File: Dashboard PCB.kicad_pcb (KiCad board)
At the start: 2 copper layers, 200 x 100 mm, 62 parts, among them J1 Controls_Leader_Export_02x06, J2 CAN, J3 INDICATOR_SWITCH_OUT, J4 FAN_CTRL_01x02, J5 Horn_In_01x02, J6 Horn_Out_01x02, J7 CAN

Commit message: Routed
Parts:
- moved +12V 12.7 mm to (105.2, 51.5)
- moved C10 12.7 mm to (107.2, 54.5)
- moved C11 12.7 mm to (103.2, 54.5)
- moved GND 12.7 mm to (105.2, 57.5)
- moved DBG_LED 6.68 mm to (91.0, 59.1)
- moved Heartbeat_LED 6.68 mm to (91.0, 55.1)
- moved R12 6.68 mm to (90.0, 51.1)
- moved D3 0.79 mm to (79.5, 113.0)
- moved FAN_CTRL 0.32 mm to (83.0, 110.0)
- moved FWD_SW 0.30 mm to (163.0, 102.5)
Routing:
- net /LFT_OUT: track 320.8 -> 223.5 mm
- net /RT_OUT: track 296.0 -> 204.3 mm
- net /FWD_SW: track 177.7 -> 118.2 mm, vias 0 -> 2
- net /CRUZ_SET: track 274.2 -> 224.0 mm, vias 0 -> 2
- net /CRUZ_EN: track 184.1 -> 228.0 mm, vias 0 -> 2
- net /BPS_HZD: track 278.8 -> 254.5 mm
- net /IGN_PWR: track 195.6 -> 219.0 mm
- net /CANGND: track 17.8 -> 0.00 mm
- net /CAN+12V: track 17.8 -> 0.00 mm
- net /FAN+: track 26.7 -> 9.70 mm
- net /CAN-H: track 16.5 -> 0.00 mm
- net /FAN-: track 22.2 -> 5.77 mm
- net /CAN-L: track 16.2 -> 0.00 mm
- net /IGN_ARR: track 232.0 -> 220.5 mm
- net /DBG_LED: track 13.8 -> 22.2 mm
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- added copper zone on F.Cu, net /CAN+12V
- added copper zone on F.Cu, net /CAN-H
- added copper zone on B.Cu, net /CAN-L
- added copper zone on B.Cu, net /CANGND
- added copper zone on F.Cu, net /FAN+
- added copper zone on B.Cu, net /FAN-

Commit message: changed routing
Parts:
- moved C3 14.9 mm to (164.2, 101.5), turned to -90 degrees
- moved C4 14.4 mm to (164.2, 109.8), turned to -90 degrees
- moved REV_SW 12.0 mm to (151.0, 108.8)
- moved FWD_SW 12.0 mm to (151.0, 102.5)
- moved R4 11.4 mm to (161.2, 109.8), turned to -90 degrees
- moved R3 11.3 mm to (161.2, 101.5), turned to -90 degrees
- moved IGN_ARR 4.61 mm to (231.5, 92.0)
- moved C5 2.75 mm to (228.2, 93.0)
- moved R5 2.00 mm to (224.0, 93.0)
- moved C6 1.60 mm to (218.0, 91.8)
- moved IGN_PWR 1.03 mm to (212.0, 86.8)
- moved R6 1.03 mm to (214.8, 89.0)
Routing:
- net /IGN_ARR: track 220.5 -> 217.4 mm
- net /IGN_PWR: track 219.0 -> 216.5 mm
- net /FWD_SW: track 118.2 -> 119.8 mm
- net /REV_SW: track 127.1 -> 126.4 mm

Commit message: More stuff
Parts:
- J2: value CAN -> Conn_02x03_CAN
- J7: value CAN -> Conn_02x03_CAN; footprint Connector_Molex:Molex_Micro-Fit_3.0_43045-0600_2x03_P3.00mm_Horizontal -> Connector_Molex:Molex_Micro-Fit_3.0_43045-0400_2x02_P3.00mm_Horizontal
- moved J7 2.00 mm to (74.0, 98.0)
- moved J2 0.75 mm to (74.0, 81.8)
- moved J4 0.50 mm to (74.0, 126.5)
- renumbered DASH_FAN to DASH_FAN1, FWD_SW to FWD_SW1, Heartbeat_LED to Heartbeat, REV_SW to REV_SW1
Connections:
- J7 pad 1: unconnected-(J7-Pin_1-Pad1) -> /CANGND
- J7 pad 2: /CANGND -> /CAN+12V
- J7 pad 3: /CAN+12V -> /CAN-L
- J7 pad 4: unconnected-(J7-Pin_4-Pad4) -> /CAN-H
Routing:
- net /BPS_HZD: track 254.5 -> 259.1 mm

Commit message: Filter move >:(
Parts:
- moved +12V 34.1 mm to (80.5, 75.0), turned to 90 degrees
- moved C10 30.1 mm to (83.5, 73.0), turned to 0 degrees
- moved C11 29.9 mm to (83.5, 77.0), turned to 0 degrees
- moved GND 25.6 mm to (86.5, 75.0), turned to 90 degrees
- moved DBG_LED 0.06 mm to (91.0, 59.0)
- moved Heartbeat 0.06 mm to (91.0, 55.0)
- moved R12 0.06 mm to (90.0, 51.0)
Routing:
- net /DBG_LED: track 22.2 -> 22.8 mm

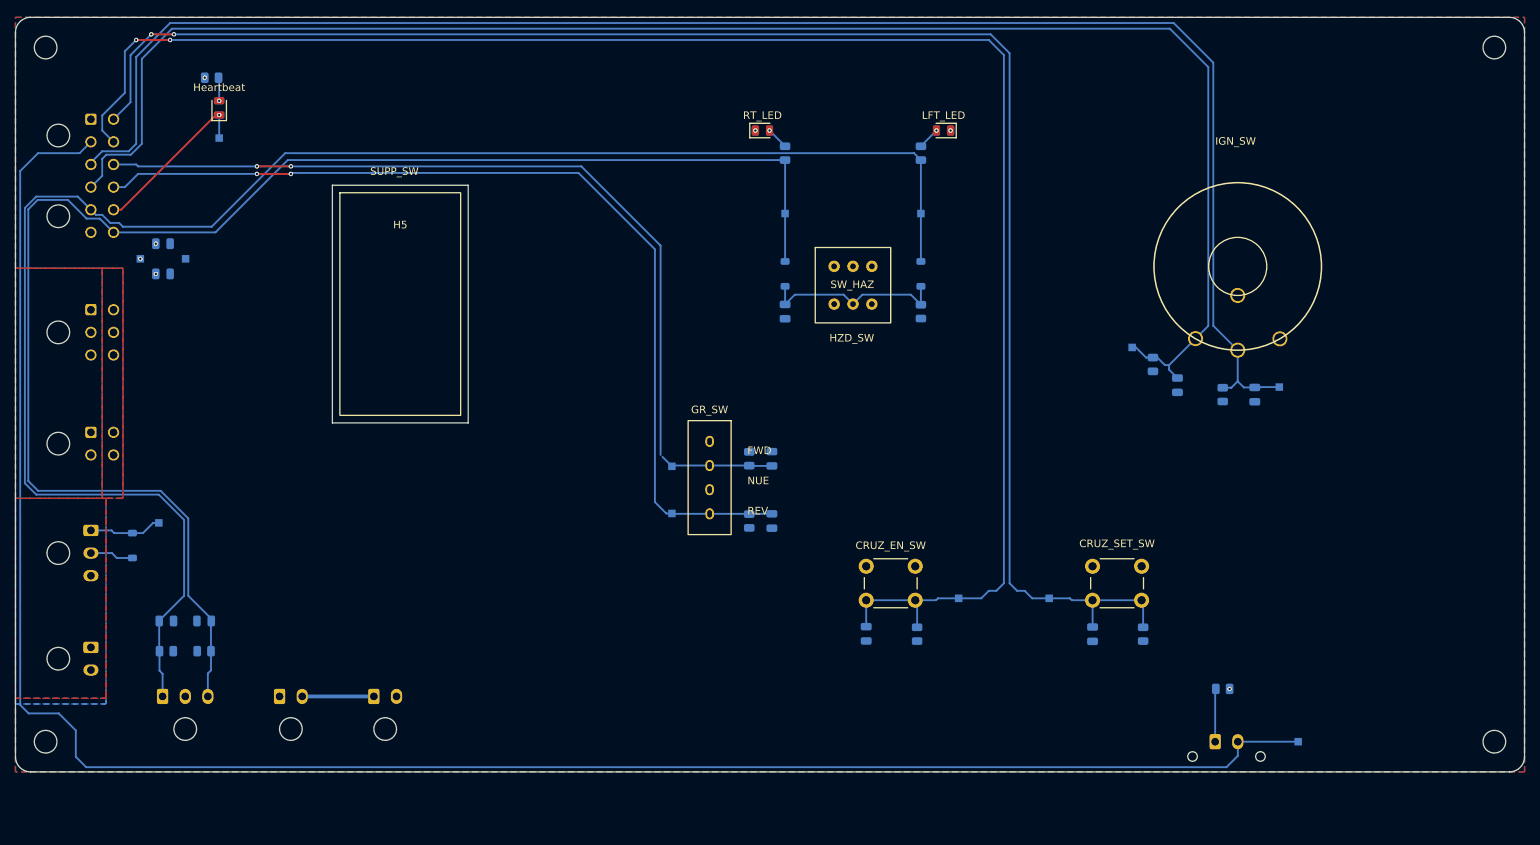
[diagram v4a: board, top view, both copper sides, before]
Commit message: Changed size and rerouted
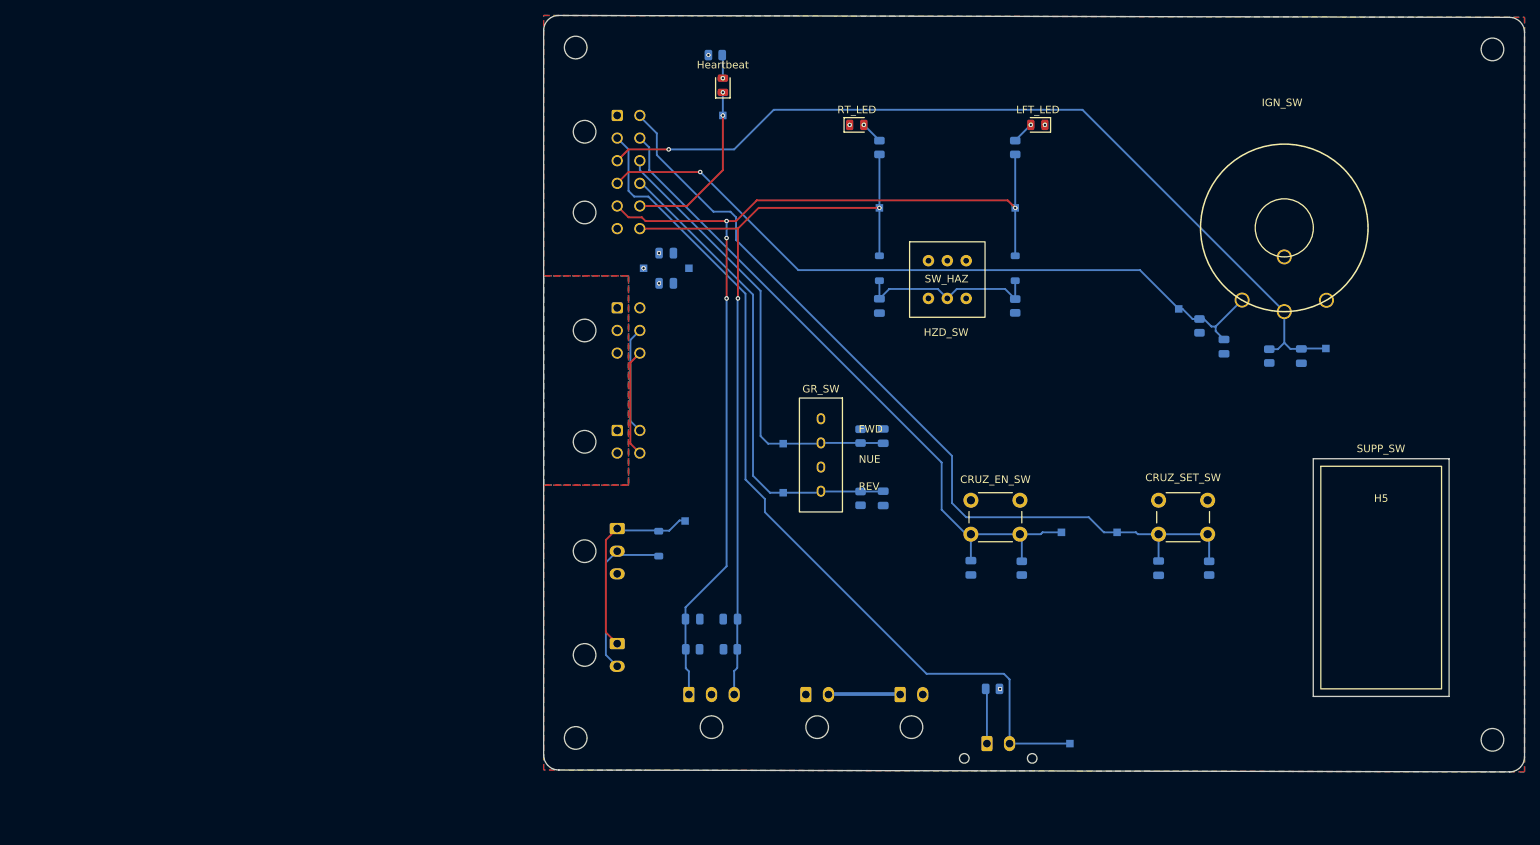
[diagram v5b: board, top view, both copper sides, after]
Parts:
- moved H5 135.0 mm to (245.0, 117.2)
- moved H3 70.3 mm to (138.2, 138.5)
- moved H1 70.2 mm to (138.2, 47.0)
- moved J1 69.8 mm to (143.8, 56.0)
- moved J4 69.8 mm to (143.8, 126.0)
- moved C1 69.8 mm to (153.8, 122.8)
- moved C2 69.8 mm to (158.8, 122.8)
- moved D3 69.8 mm to (149.2, 112.8)
- moved DASH_FAN1 69.8 mm to (143.8, 110.8)
- moved FAN_CTRL 69.8 mm to (152.8, 109.8)
- moved J2 69.8 mm to (143.8, 81.5)
- moved J3 69.8 mm to (153.2, 132.8)
- moved J5 69.8 mm to (168.8, 132.8)
- moved J6 69.8 mm to (181.2, 132.8)
- moved J7 69.8 mm to (143.8, 97.8)
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- renumbered FWD_SW1 to FWD_SW, REV_SW1 to REV_SW
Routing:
- net /BPS_HZD: track 259.1 -> 116.9 mm
- net /CRUZ_EN: track 227.9 -> 90.3 mm, vias 2 -> 0
- net /IGN_PWR: track 216.5 -> 95.5 mm, vias 0 -> 1
- net /CRUZ_SET: track 224.0 -> 112.6 mm, vias 2 -> 0
- net /IGN_ARR: track 217.4 -> 114.8 mm, vias 0 -> 1
- net /RT_OUT: track 204.3 -> 108.3 mm, vias 0 -> 2
- net /LFT_OUT: track 223.4 -> 133.8 mm, vias 0 -> 4
- net /REV_SW: track 126.4 -> 63.6 mm, vias 2 -> 0
- net /FWD_SW: track 119.8 -> 60.5 mm, vias 2 -> 0
- net /FAN+: track 9.70 -> 26.2 mm
- net /FAN-: track 5.77 -> 22.3 mm
- net /CAN-L: track 0.00 -> 14.3 mm
- net /CAN-H: track 0.00 -> 14.3 mm
- net /DBG_LED: track 22.8 -> 24.2 mm, vias 1 -> 2
- removed copper zone on F.Cu, net /CAN-H
- removed copper zone on B.Cu, net /CAN-L
- removed copper zone on F.Cu, net /FAN+
- removed copper zone on B.Cu, net /FAN-
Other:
- board size 200 x 100 mm -> 130 x 100.2 mm
- board text added: "13cm x 10cm"
- board text removed: "20cm x 10cm"

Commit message: Labled n other stuff
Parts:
- renumbered IGN_PWR to IGN_MTR
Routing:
- net /CRUZ_SET: track 112.6 -> 111.3 mm
- net /LFT_OUT: track 133.8 -> 134.8 mm
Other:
- outline, holes or cut-outs redrawn
- board text added: "+ -"
- board text added: "+12V"
- board text added: "12V"
- board text added: "BPS_HZD"
- board text added: "CAN-H CAN-L"
- board text added: "CAN-H CAN-L CANPWR CANGND"
- board text added: "CANGND CANPWR"
- board text added: "GND"
- board text added: "LFT"
- board text added: "LFT_OUT IGN_MTR IGN_ARR BPS_HZD"
- board text added: "Mounting pt for BPS led (Still need dimensions)"
- board text added: "RT"
- board text added: "RT_OUT DBG_LED REV_SW FWD_SW CRUZ_EN CRUZ_SET"
- board text added: "RT_OUT DBG_LED REV_SW FWD_SW CRZ_EN CRZ_SET GND LFT_OUT IGN_MTR IGN_ARR BPS_HZD +12V"
- board text added: "X"
- board text added: "X X"

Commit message: A bunch of stuff
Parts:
- removed BPS_HZD_OUT: BPS_HAZARD_LIGHT, Connector_Molex:Molex_Micro-Fit_3.0_43650-0215_1x02_P3.00mm_Vertical
- added BPS_HZD_LED: SMD_0805_RED, LED_SMD:LED_0805_2012Metric, F.Cu at (137.0, 59.5)
- added J8: Supp_Out, Connector_Molex:Molex_Micro-Fit_3.0_43650-0200_1x02_P3.00mm_Horizontal, B.Cu at (200.8, 141.0)
- added Supp Sw Connectors: Supp_In, Connector_Molex:Molex_Micro-Fit_3.0_43650-0215_1x02_P3.00mm_Vertical, B.Cu at (220.2, 144.5)
- C10, C11: moved to F.Cu
- moved BPS_HZD 106.1 mm to (137.0, 56.8)
- moved R13 89.2 mm to (141.5, 59.5)
- moved C11 61.8 mm to (89.0, 69.6), turned to 180 degrees
- moved C10 61.2 mm to (89.0, 72.8)
- moved GND 57.2 mm to (96.3, 81.3)
- moved C5 56.8 mm to (178.0, 94.2)
- moved C6 56.8 mm to (167.8, 93.0)
- moved IGN_ARR 56.8 mm to (181.2, 93.2)
- moved IGN_MTR 56.8 mm to (161.8, 88.0)
- moved IGN_SW1 56.8 mm to (175.8, 77.2)
- moved R5 56.8 mm to (173.8, 94.2)
- moved R6 56.8 mm to (164.5, 90.2)
- moved +12V 53.2 mm to (96.3, 60.8)
- moved Heartbeat 51.1 mm to (107.2, 59.5)
- moved C1 51.0 mm to (103.3, 130.3)
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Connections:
- net /IGN_PWR renamed /IGN_MTR
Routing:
- net /BPS_HZD: track 116.9 -> 48.8 mm, vias 0 -> 1
- net /IGN_MTR: track 95.5 -> 89.1 mm
- net /IGN_ARR: track 114.8 -> 109.2 mm
- net Net-(BPS_HZD_LED1-A): track 7.28 -> 3.00 mm, vias 0 -> 1
- net GND: vias 2 -> 4
- net +12V: vias 5 -> 3
- added copper zone on F.Cu, net /Supp+
- added copper zone on B.Cu, net /Supp-
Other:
- board size 130 x 100.2 mm -> 150 x 100.2 mm
- board text added: "- +"
- board text removed: "Approx 3d model"
- board text removed: "BPS_HZD"
- board text removed: "Mounting pt for BPS led (Still need dimensions)"

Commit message: Supp changes
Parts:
- added R14: 5.1k, Resistor_SMD:R_0805_2012Metric, B.Cu at (203.0, 59.8)
- added SUPP_ON: LED, LED_SMD:LED_0805_2012Metric, F.Cu at (198.5, 59.8)
- J8: footprint Connector_Molex:Molex_Micro-Fit_3.0_43650-0200_1x02_P3.00mm_Horizontal -> Connector_Molex:Molex_Micro-Fit_3.0_43650-0300_1x03_P3.00mm_Horizontal
- J9: renamed from Supp Sw Connectors
- moved DBG_LED 86.0 mm to (193.3, 63.9)
- moved Heartbeat 86.0 mm to (193.2, 59.8)
- moved R12 86.0 mm to (192.2, 55.8)
- moved BPS_HZD 51.3 mm to (188.2, 59.8), turned to 90 degrees
- moved R13 45.9 mm to (187.2, 55.8), turned to 0 degrees
- moved BPS_HZD 45.2 mm to (182.0, 60.8)
- moved CRUZ_EN 5.91 mm to (152.2, 124.8)
- moved CRUZ_SET 5.91 mm to (159.5, 124.8)
- moved C8 5.91 mm to (165.0, 129.5)
- moved C9 5.91 mm to (140.2, 129.4)
- moved CRUZ_EN_SW 5.91 mm to (140.2, 120.5)
- moved CRUZ_SET_SW 5.91 mm to (165.0, 120.5)
- moved R8 5.91 mm to (171.8, 129.5)
- moved R9 5.91 mm to (146.9, 129.5)
- moved C5 5.24 mm to (177.0, 99.4)
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- renumbered BPS_HZD_LED to BPS_HZD, HZD_SW to HZD_SW1, IGN_MTR to IGN_PWR
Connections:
- J8 pad 2: /Supp- -> /LV_EN
- J9 pad 2: /Supp- -> /LV_EN
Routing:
- net /Supp-: track 0.00 -> 83.7 mm, vias 0 -> 1
- net /DBG_LED: track 24.2 -> 106.0 mm
- net /BPS_HZD: track 48.8 -> 97.4 mm
- net /CRUZ_EN: track 90.3 -> 96.5 mm
- net /CRUZ_SET: track 111.3 -> 117.2 mm
- net Net-(D4-A): track 0.00 -> 4.84 mm, vias 0 -> 1
- net /IGN_ARR: track 109.2 -> 113.4 mm
- net /IGN_MTR: track 89.1 -> 90.2 mm
- added copper zone on B.Cu, net /LV_EN
- removed copper zone on B.Cu, net /Supp-
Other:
- outline, holes or cut-outs redrawn
- board text added: "- LV_EN +"
- board text added: "Supp+ LV_EN"
- board text removed: "- +"
